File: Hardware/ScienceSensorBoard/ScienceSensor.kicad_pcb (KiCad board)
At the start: 2 copper layers, 101.6 x 76.2 mm, 92 parts, among them J1 Conn_02x03_Counter_Clockwise, J2 RJ45_LED_Shielded, Q1 SI4156DY, Q10 BSS138, Q11 SI4156DY, Q2 SI4156DY, Q3 SI4156DY, Q4 BSS138, Q5 BSS138, Q6 BSS138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

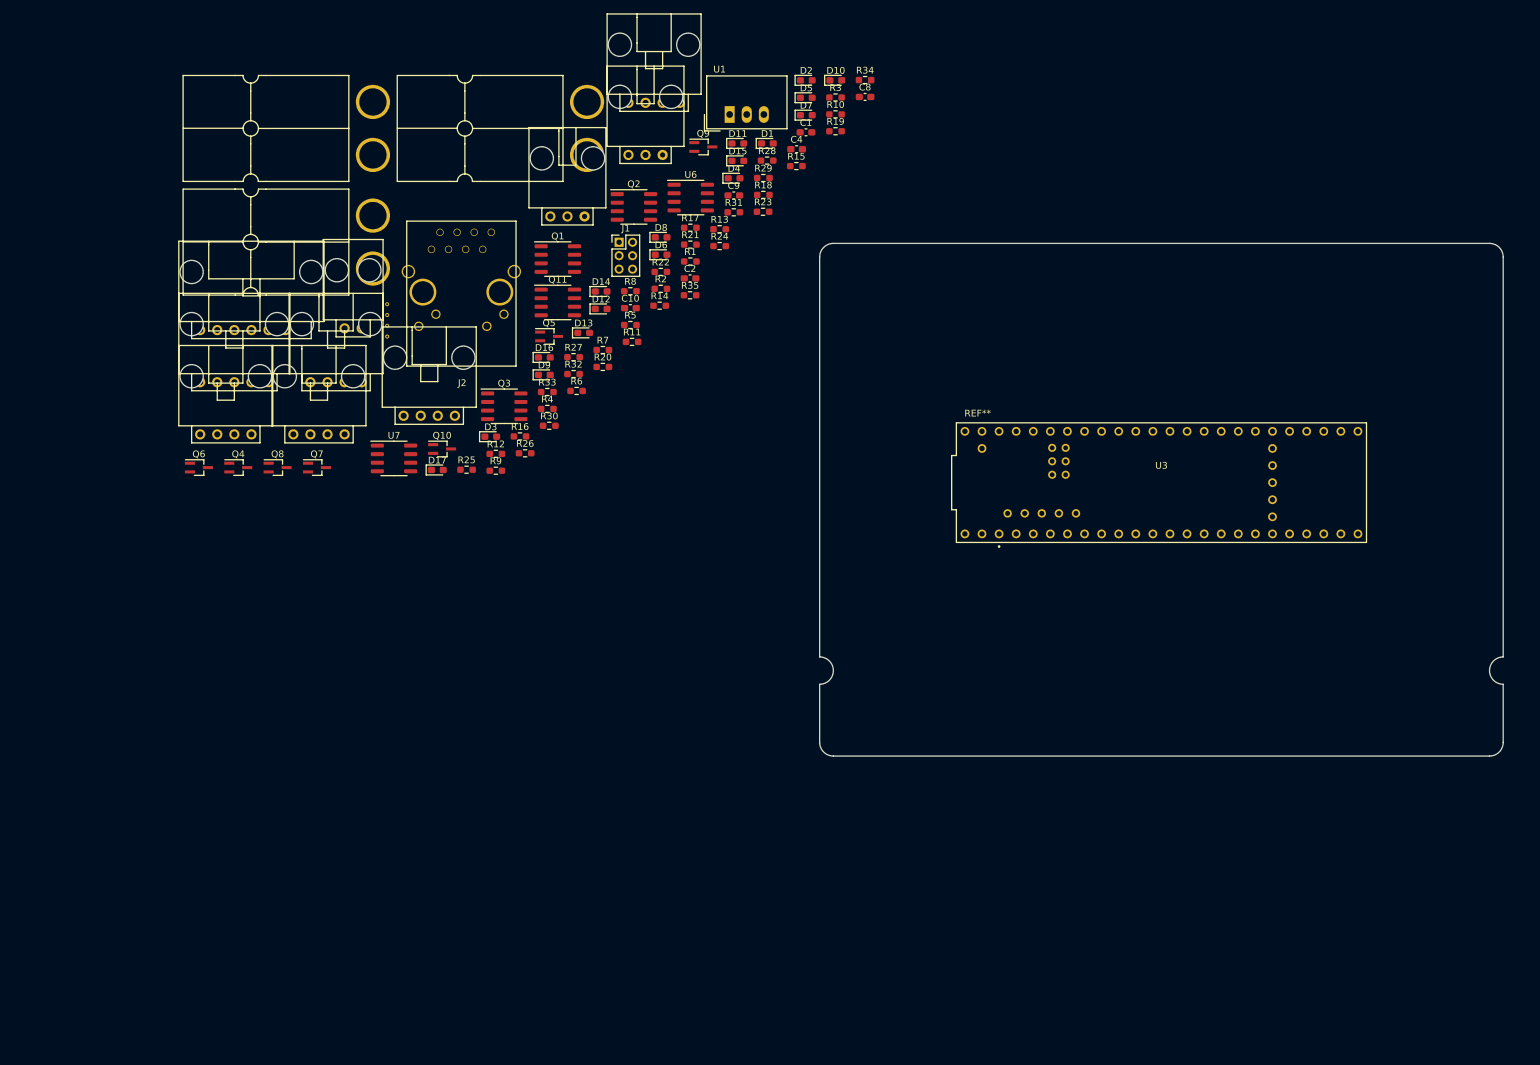
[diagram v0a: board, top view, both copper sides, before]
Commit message: Sensor Layout organization.
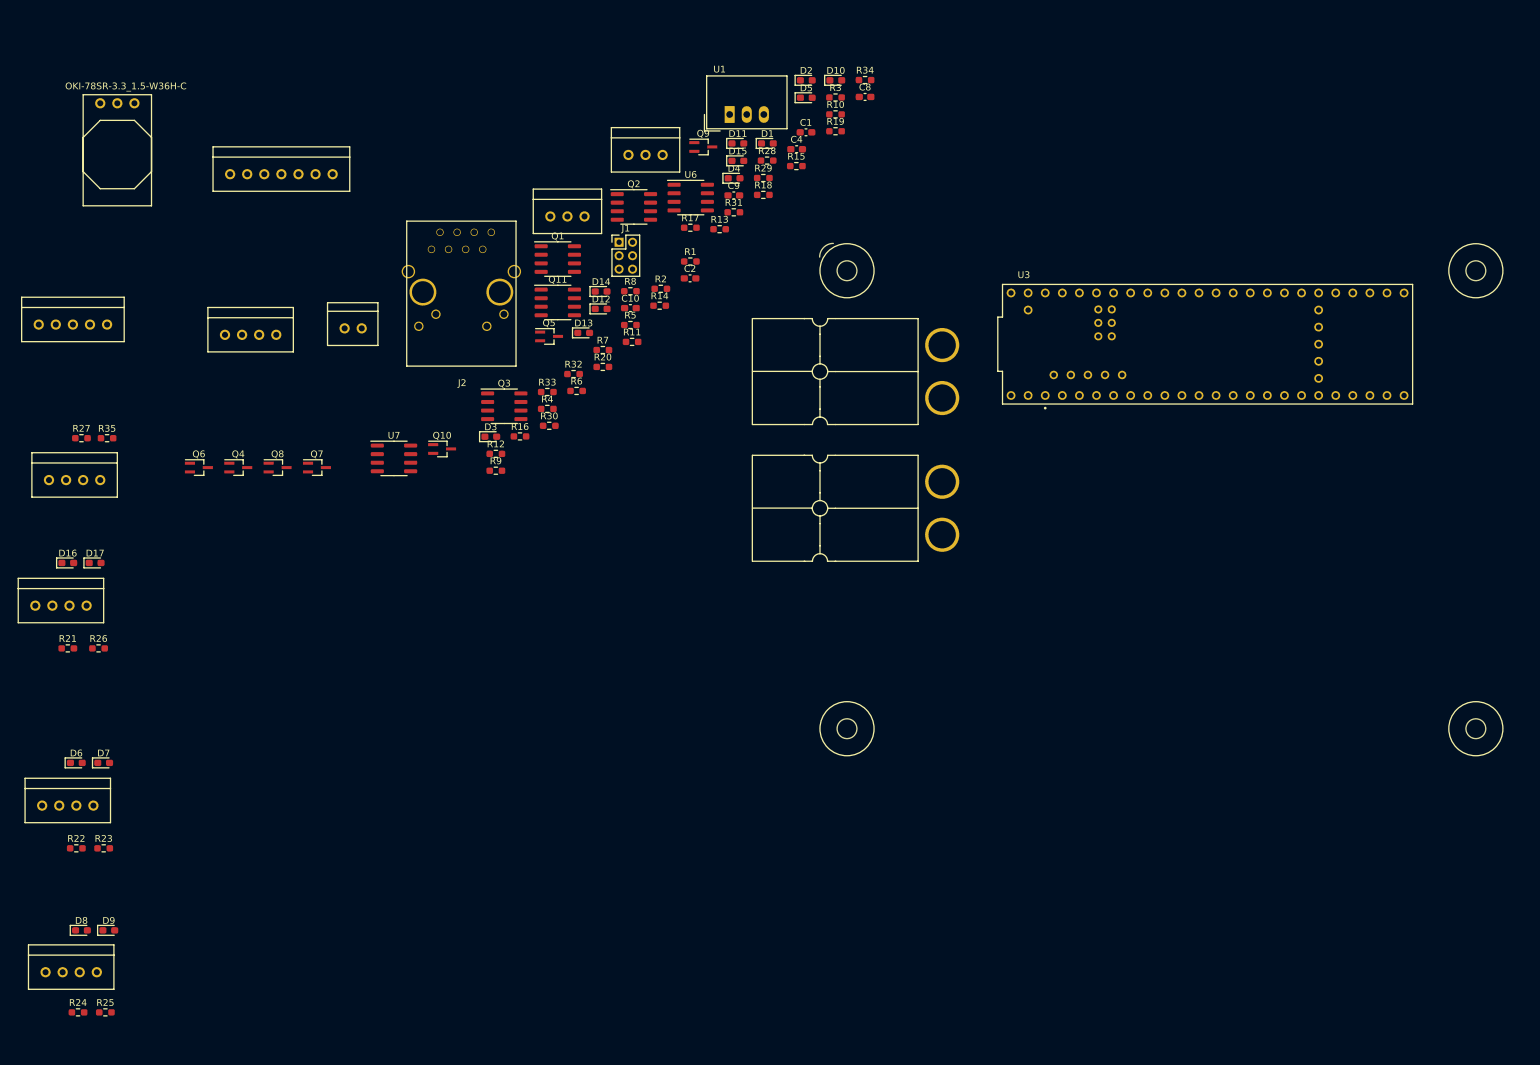
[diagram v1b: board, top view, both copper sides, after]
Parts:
- removed Conn2: AndersonPP, MRDT_Connectors:Anderson_2_Horizontal_Side_by_Side
- added U2: OKI-78SR-3.3_1.5-W36H-C, MRDT_Devices:OKI_Horizontal, F.Cu at (36.6, 41.4)
- Conn10: footprint MRDT_Connectors:MOLEX_SL_05_Horizontal -> MRDT_Connectors:MOLEX_SL_05_Vertical
- Conn11, Conn13, Conn7, Conn8, Conn9: footprint MRDT_Connectors:MOLEX_SL_04_Horizontal -> MRDT_Connectors:MOLEX_SL_04_Vertical
- Conn12, Conn6: footprint MRDT_Connectors:MOLEX_SL_03_Horizontal -> MRDT_Connectors:MOLEX_SL_03_Vertical
- Conn3: footprint MRDT_Connectors:MOLEX_SL_02_Horizontal -> MRDT_Connectors:MOLEX_SL_02_Vertical
- Conn4: footprint MRDT_Connectors:MOLEX_SL_07_Horizontal -> MRDT_Connectors:MOLEX_SL_07_Vertical
- U3: footprint MRDT_Shields:Teensy_4_1_Vertical -> MRDT_Shields:Teensy_4_1
- V1, V2, V3, V4: footprint MRDT_Drill_Holes:Via_.6mm -> MRDT_Drill_Holes:4_40_Hole
- moved V3 172.0 mm to (241.0, 134.4)
- moved V2 162.0 mm to (241.0, 66.3)
- moved Conn9 155.6 mm to (28.4, 170.6)
- moved R24 148.6 mm to (33.3, 176.5)
- moved D7 142.0 mm to (37.1, 139.4)
- moved R23 136.2 mm to (37.1, 152.1)
- moved D8 134.3 mm to (33.8, 164.3)
- moved R22 122.0 mm to (33.0, 152.1)
- moved D6 115.2 mm to (33.0, 139.4)
- moved R21 110.3 mm to (31.8, 122.4)
- moved D9 104.9 mm to (37.8, 164.3)
- moved R25 96.9 mm to (37.3, 176.5)
- moved Conn1 92.0 mm to (161.7, 77.3)
- moved V4 90.9 mm to (147.6, 134.4)
- moved R35 89.2 mm to (37.6, 91.2)
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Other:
- board size 101.6 x 76.2 mm -> 2 x 2 mm

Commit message: Mosfets & H-Bridge Organized, Photodiode organized, Footprints for LED
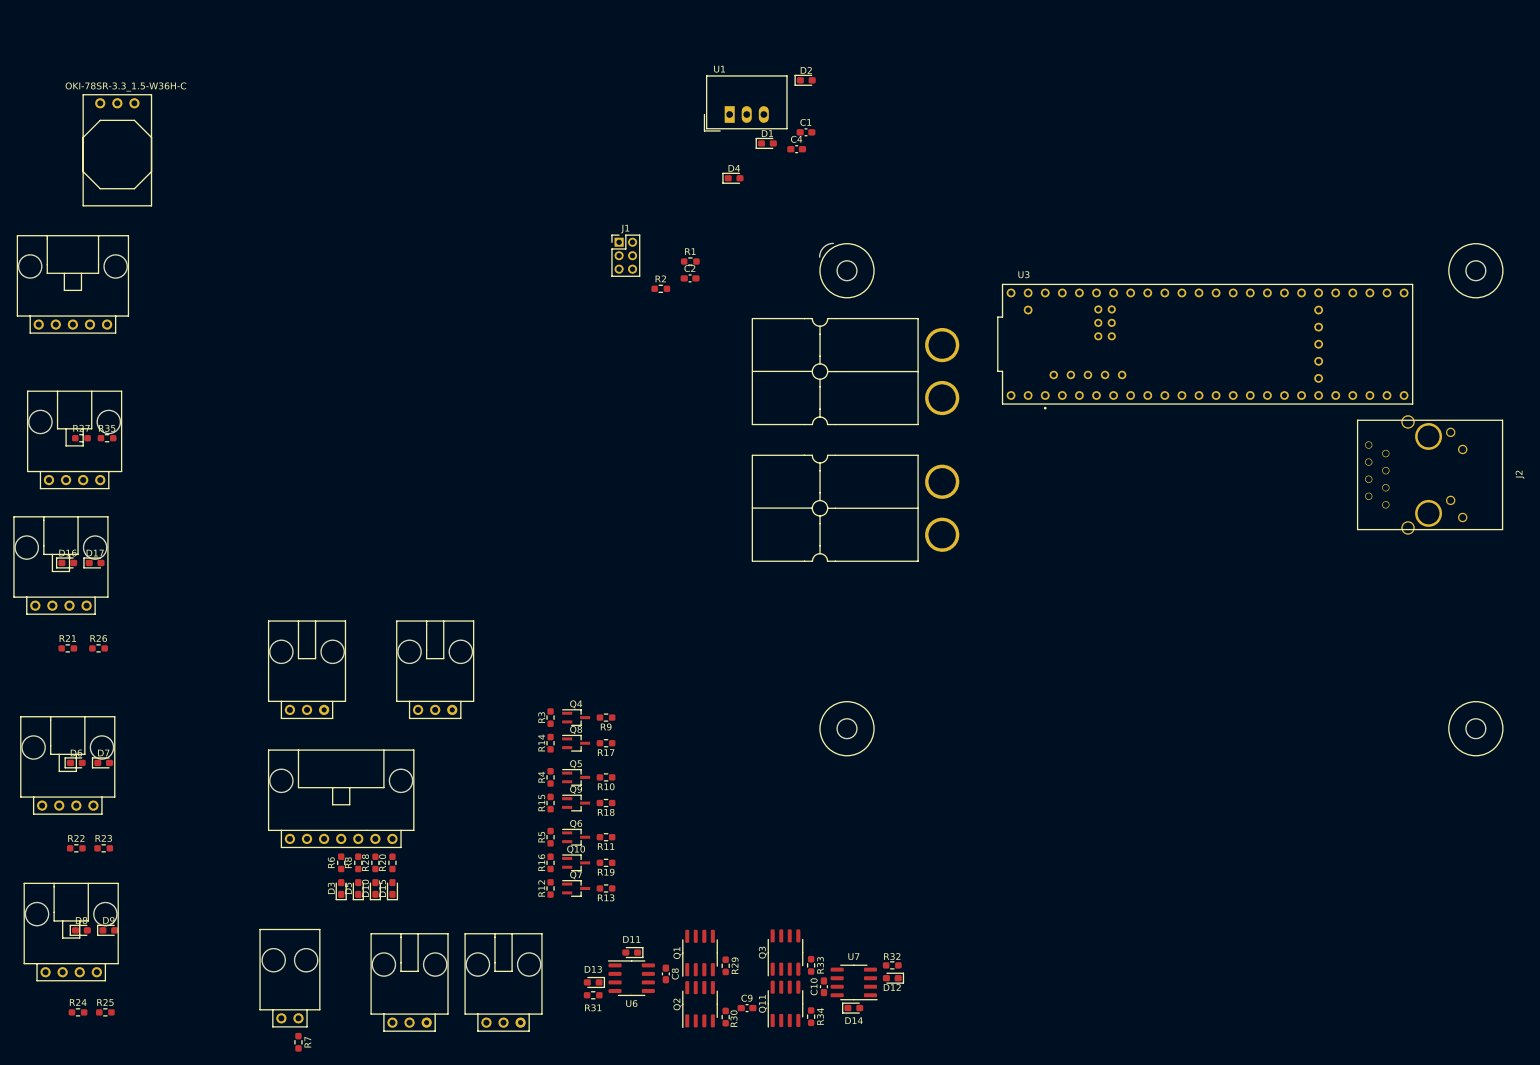
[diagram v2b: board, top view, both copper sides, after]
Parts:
- added Conn2: Molex_SL_03, MRDT_Connectors:MOLEX_SL_03_Horizontal, F.Cu at (83.8, 131.6)
- Conn10: footprint MRDT_Connectors:MOLEX_SL_05_Vertical -> MRDT_Connectors:MOLEX_SL_05_Horizontal
- Conn11, Conn13, Conn8, Conn9: footprint MRDT_Connectors:MOLEX_SL_04_Vertical -> MRDT_Connectors:MOLEX_SL_04_Horizontal
- Conn12, Conn6: footprint MRDT_Connectors:MOLEX_SL_03_Vertical -> MRDT_Connectors:MOLEX_SL_03_Horizontal
- Conn3: footprint MRDT_Connectors:MOLEX_SL_02_Vertical -> MRDT_Connectors:MOLEX_SL_02_Horizontal
- Conn4: footprint MRDT_Connectors:MOLEX_SL_07_Vertical -> MRDT_Connectors:MOLEX_SL_07_Horizontal
- Conn7: value Molex_SL_04 -> Molex_SL_03; footprint MRDT_Connectors:MOLEX_SL_04_Vertical -> MRDT_Connectors:MOLEX_SL_03_Horizontal
- moved J2 157.3 mm to (247.0, 96.5), turned to 90 degrees
- moved R34 139.4 mm to (142.2, 177.2), turned to -90 degrees
- moved D10 138.3 mm to (77.5, 158.1), turned to 90 degrees
- moved D5 135.1 mm to (74.9, 158.1), turned to 90 degrees
- moved C8 133.7 mm to (120.7, 170.8), turned to -90 degrees
- moved Conn6 130.7 mm to (94.0, 178.1)
- moved Conn12 122.1 mm to (80.0, 178.1)
- moved D11 121.3 mm to (115.6, 167.6), turned to 180 degrees
- moved C9 120.8 mm to (132.7, 175.9)
- moved D15 119.7 mm to (80.0, 158.1), turned to 90 degrees
- moved R28 119.5 mm to (77.5, 154.3), turned to 90 degrees
- moved Q2 118.9 mm to (125.7, 175.3), turned to 90 degrees
- moved R31 118.2 mm to (109.9, 174.0)
- moved R29 117.2 mm to (129.5, 169.6), turned to -90 degrees
- moved U6 116.4 mm to (115.6, 171.4)
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
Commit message: Layout Organization
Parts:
- moved V1 0.25 mm to (147.3, 66.3)
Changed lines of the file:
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@@
   )
   (footprint "MRDT_Drill_Holes:4_40_Hole" (layer "F.Cu")
-    (at 147.574 66.294)
+    (at 147.32 66.294)
     (property "Sheetfile" "ScienceSensor.kicad_sch")
     (property "Sheetname" "")

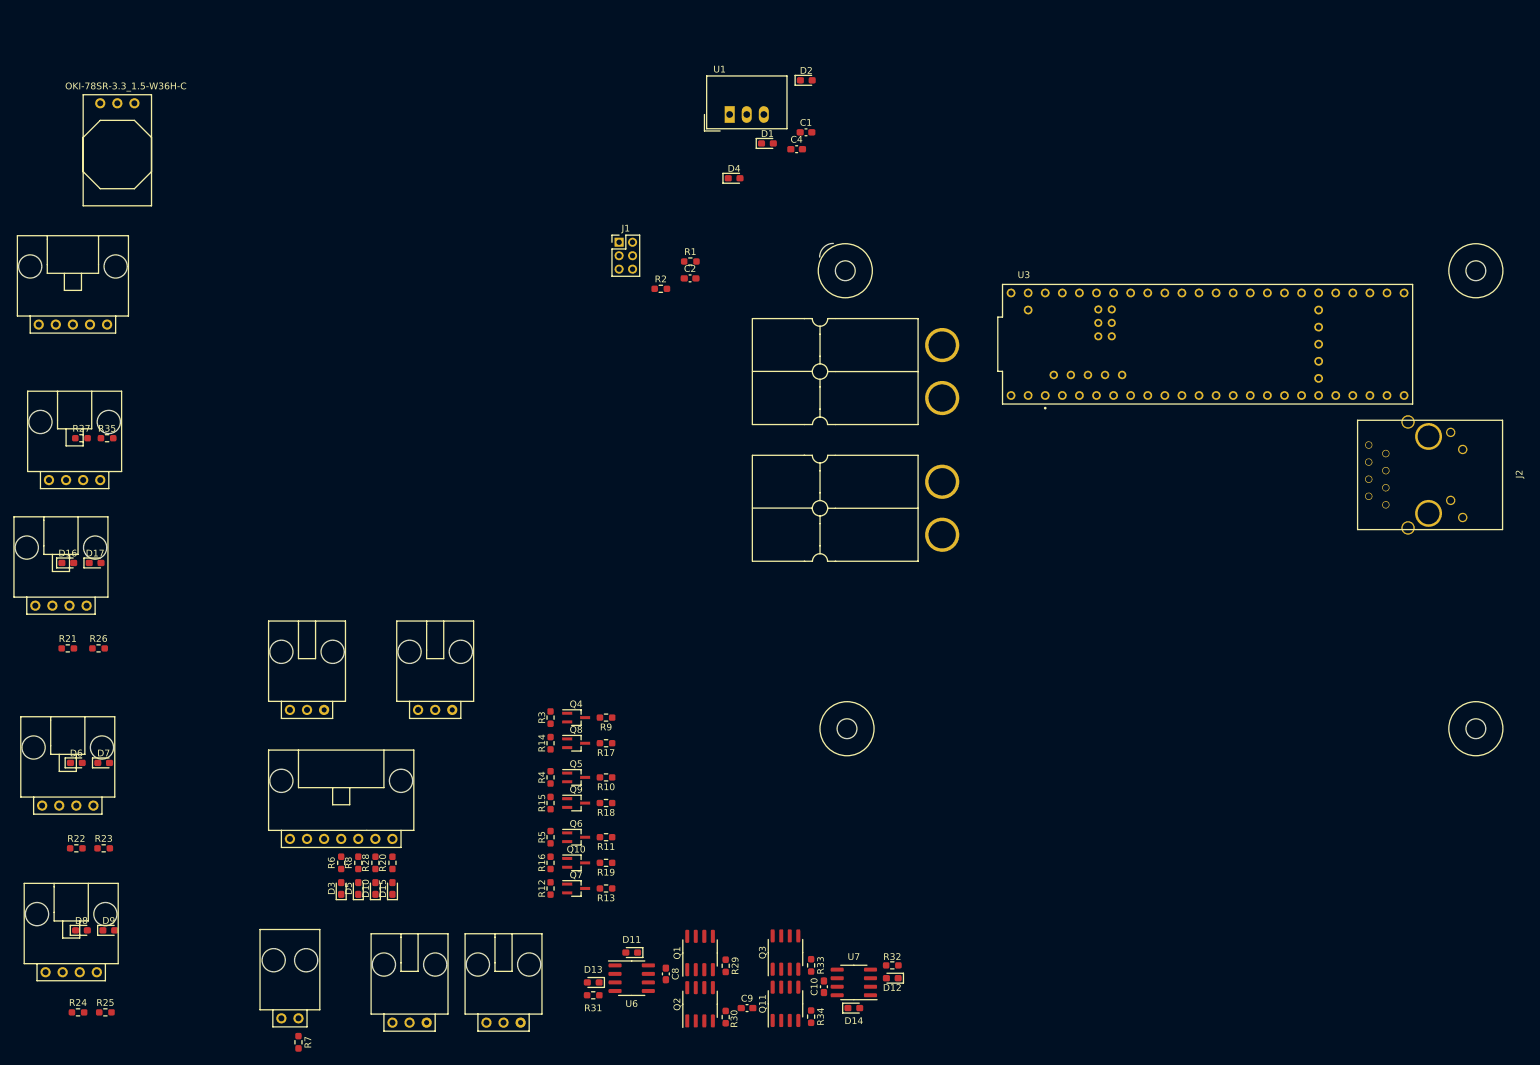
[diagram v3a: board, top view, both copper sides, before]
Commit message: Sensor board layout organization
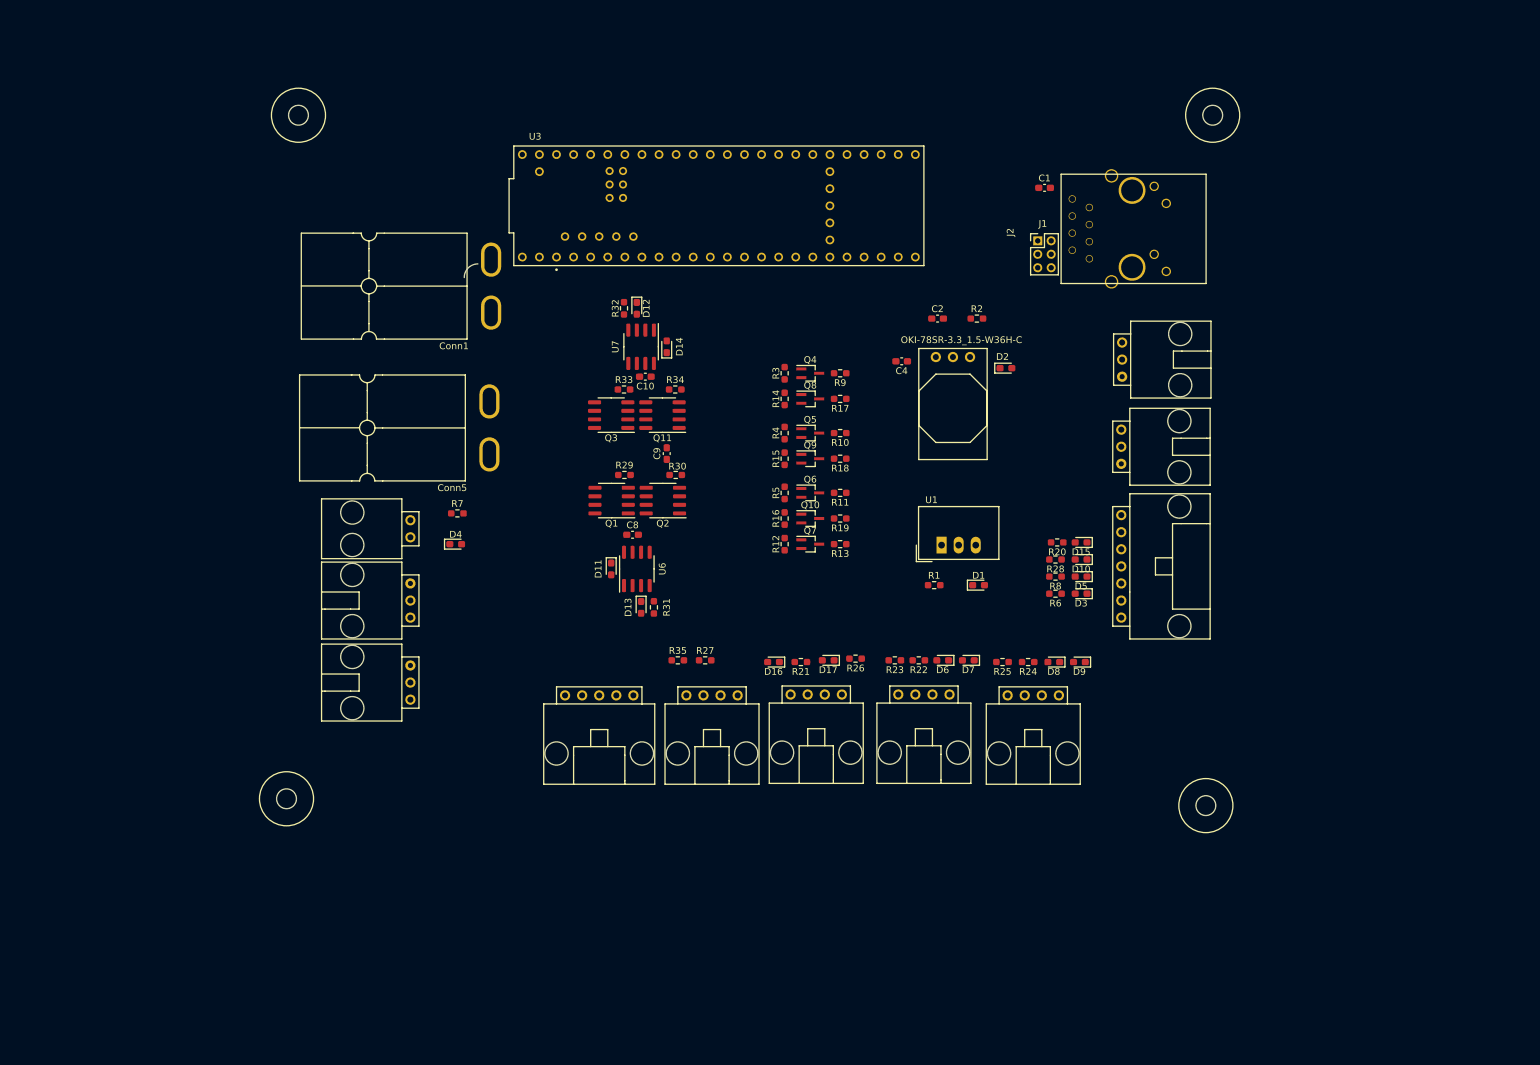
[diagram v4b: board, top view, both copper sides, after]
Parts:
- Conn1, Conn5: footprint MRDT_Connectors:Anderson_2_Horizontal_Side_by_Side -> MRDT_Connectors:Square_Anderson_2_H_Side_By_Side
- moved Conn9 156.1 mm to (179.1, 129.4), turned to 180 degrees
- moved R24 150.5 mm to (174.5, 124.5), turned to 180 degrees
- moved D8 149.9 mm to (178.3, 124.5), turned to 180 degrees
- moved D9 149.7 mm to (182.1, 124.5), turned to 180 degrees
- moved Conn12 148.3 mm to (188.5, 77.0), turned to -90 degrees
- moved R25 143.2 mm to (170.7, 124.5), turned to 180 degrees
- moved Conn8 135.9 mm to (162.8, 129.3), turned to 180 degrees
- moved Conn4 132.6 mm to (188.3, 102.6), turned to -90 degrees
- moved U2 129.8 mm to (160.8, 79.1)
- moved D6 129.7 mm to (161.8, 124.2), turned to 180 degrees
- moved D7 129.4 mm to (165.6, 124.2), turned to 180 degrees
- moved Conn6 129.1 mm to (188.3, 89.9), turned to -90 degrees
- moved R22 128.3 mm to (158.2, 124.2), turned to 180 degrees
- moved R23 120.9 mm to (154.7, 124.2), turned to 180 degrees
- moved Conn11 120.6 mm to (146.8, 129.3), turned to 180 degrees
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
